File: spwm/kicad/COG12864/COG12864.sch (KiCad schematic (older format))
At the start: 62 parts, among them J1 Conn_01x02_Male, Q4 Q_NMOS_GDS, Q5 Q_NMOS_GDS, Q6 Q_NMOS_GDS, Q7 Q_NMOS_GDS, SW1 SW_Push, SW2 SW_Push, U1 N32G430C8L7, U3 EG2131, U4 EG2131, U5 LMV722, U6 LMV722, Y1 8MHZ

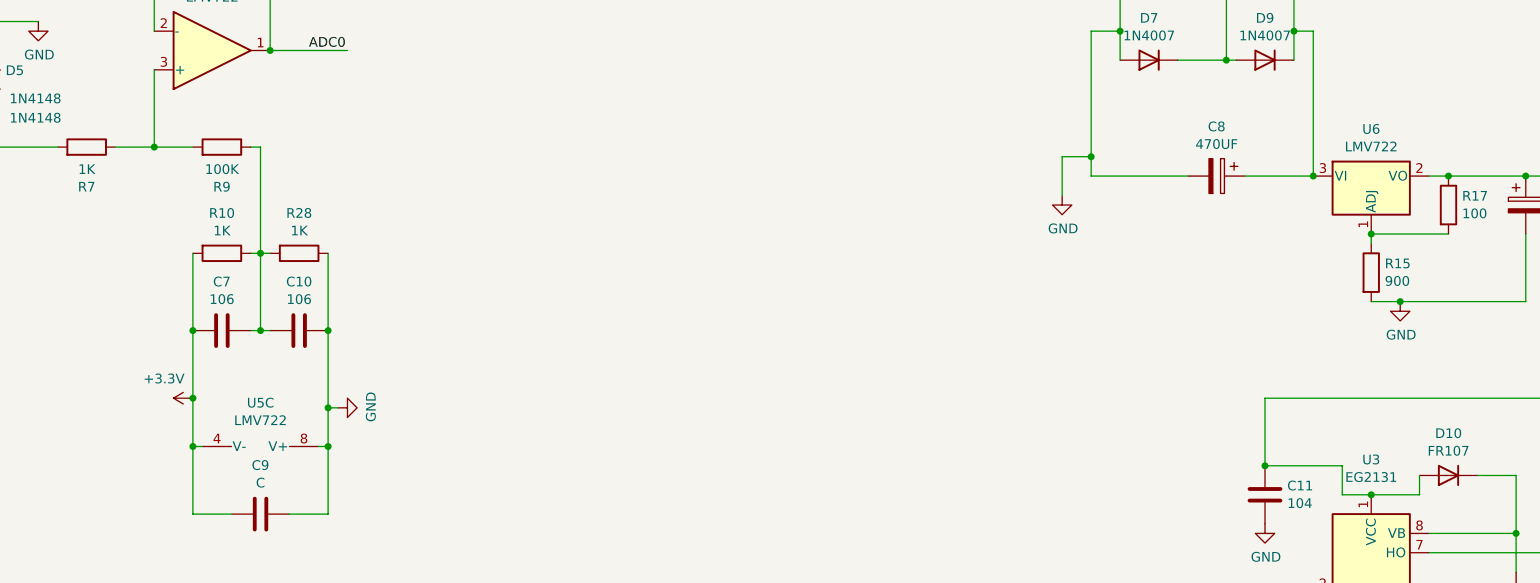
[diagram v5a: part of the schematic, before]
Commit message: 改正原理图绘制错误
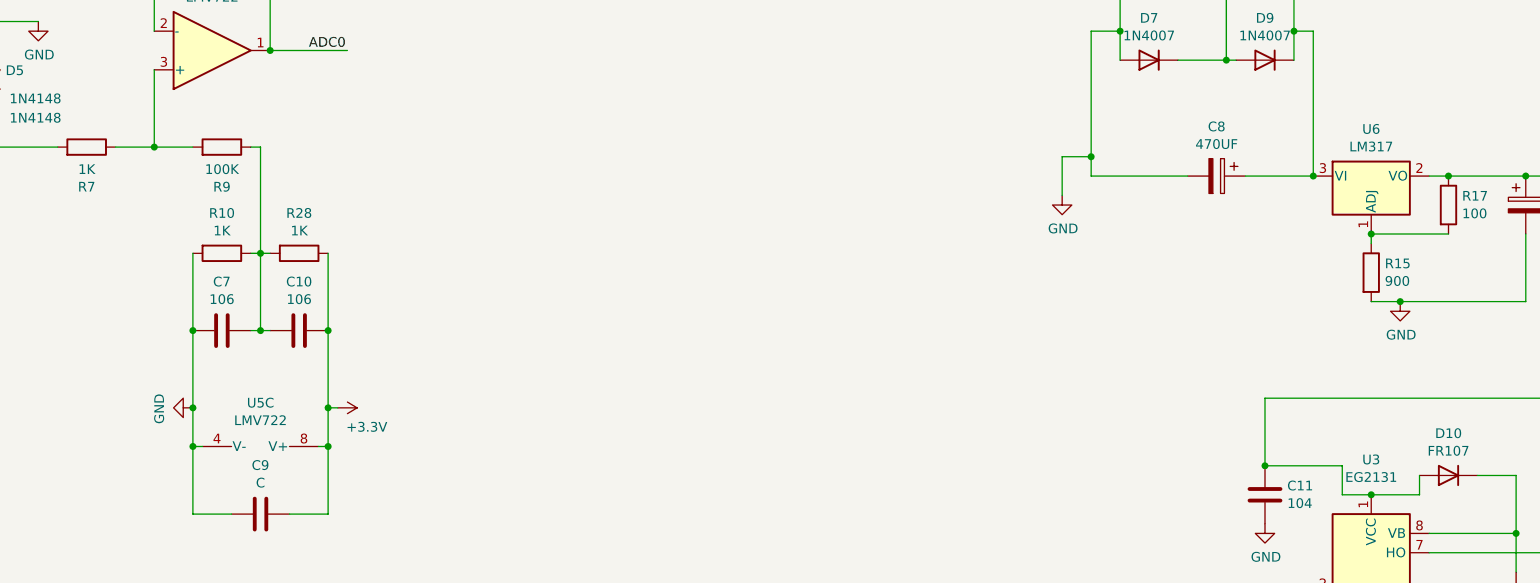
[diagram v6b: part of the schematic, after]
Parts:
- U6: value LMV722 -> LM317
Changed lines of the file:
@@
 L power:GND #PWR019
 U 1 1 62F3C1F0
+P 5350 5150
+F 0 "#PWR019" H 5350 4900 50  0001 C CNN
+F 1 "GND" H 5355 4977 50  0000 C CNN
+F 2 "" H 5350 5150 50  0001 C CNN
+F 3 "" H 5350 5150 50  0001 C CNN
+	1    5350 5150
+	0    1    1    0
+$EndComp
+$Comp
+L power:+3.3V #PWR018
+U 1 1 62F3D129
 P 6100 5150
-F 0 "#PWR019" H 6100 4900 50  0001 C CNN
-F 1 "GND" H 6105 4977 50  0000 C CNN
+F 0 "#PWR018" H 6100 5000 50  0001 C CNN
+F 1 "+3.3V" V 6200 5300 50  0000 C CNN
 F 2 "" H 6100 5150 50  0001 C CNN
 F 3 "" H 6100 5150 50  0001 C CNN
 	1    6100 5150
-	0    -1   -1   0
-$EndComp
-$Comp
-L power:+3.3V #PWR018
-U 1 1 62F3D129
-P 5350 5100
-F 0 "#PWR018" H 5350 4950 50  0001 C CNN
-F 1 "+3.3V" V 5450 5250 50  0000 C CNN
-F 2 "" H 5350 5100 50  0001 C CNN
-F 3 "" H 5350 5100 50  0001 C CNN
-	1    5350 5100
-	0    -1   -1   0
+	0    1    1    0
 $EndComp
 $Comp
@@
 Wire Wire Line
 	5400 5350 5350 5350
-Wire Wire Line
-	5350 5350 5350 5100
 Connection ~ 5350 4750
-Connection ~ 5350 5100
-Wire Wire Line
-	5350 5100 5350 4750
 $Comp
 L Device:C C9
@@
 P 11450 3950
 F 0 "U6" H 11450 4192 50  0000 C CNN
-F 1 "LMV722" H 11450 4101 50  0000 C CNN
+F 1 "LM317" H 11450 4101 50  0000 C CNN
 F 2 "" H 11450 4200 50  0001 C CIN
 F 3 "" H 11450 3950 50  0001 C CNN
@@
 Wire Wire Line
 	9950 12000 9950 12700
+Wire Wire Line
+	5350 4750 5350 5150
+Connection ~ 5350 5150
+Wire Wire Line
+	5350 5150 5350 5350
 $EndSCHEMATC

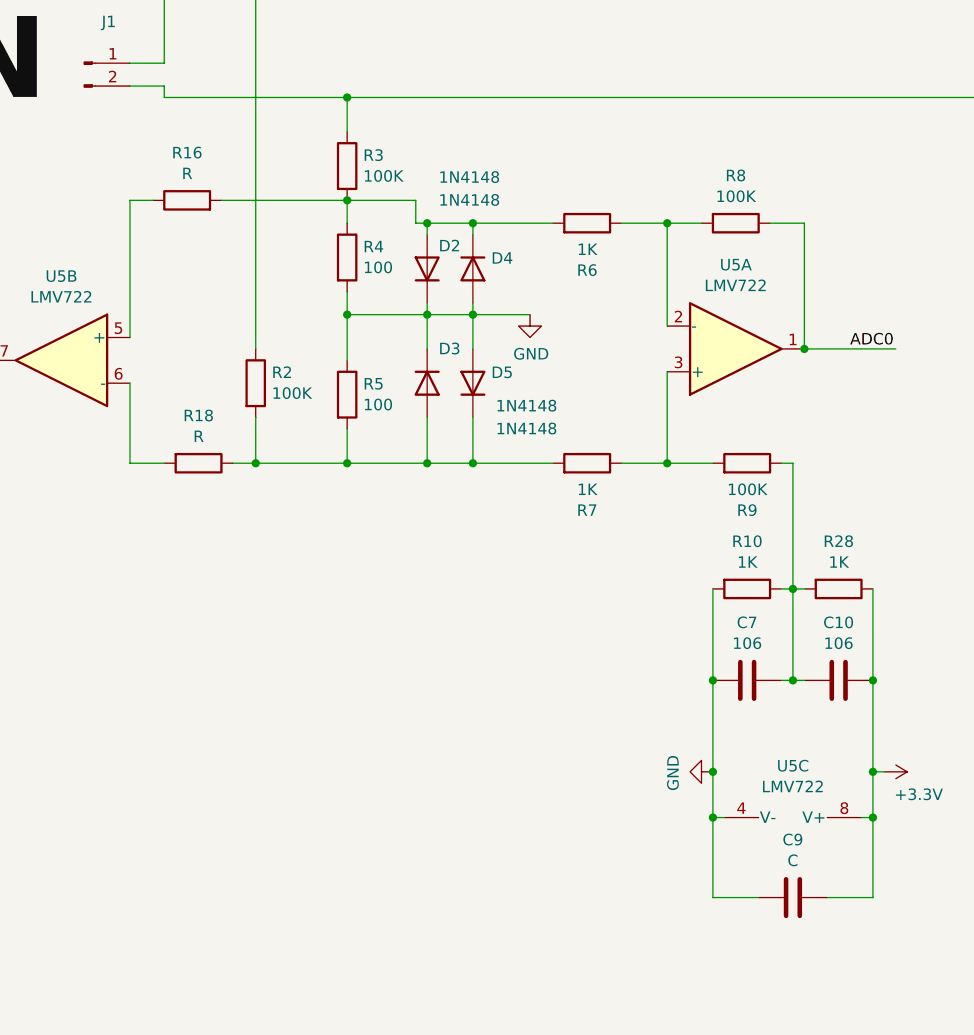
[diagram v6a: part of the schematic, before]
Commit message: 修改按键错误
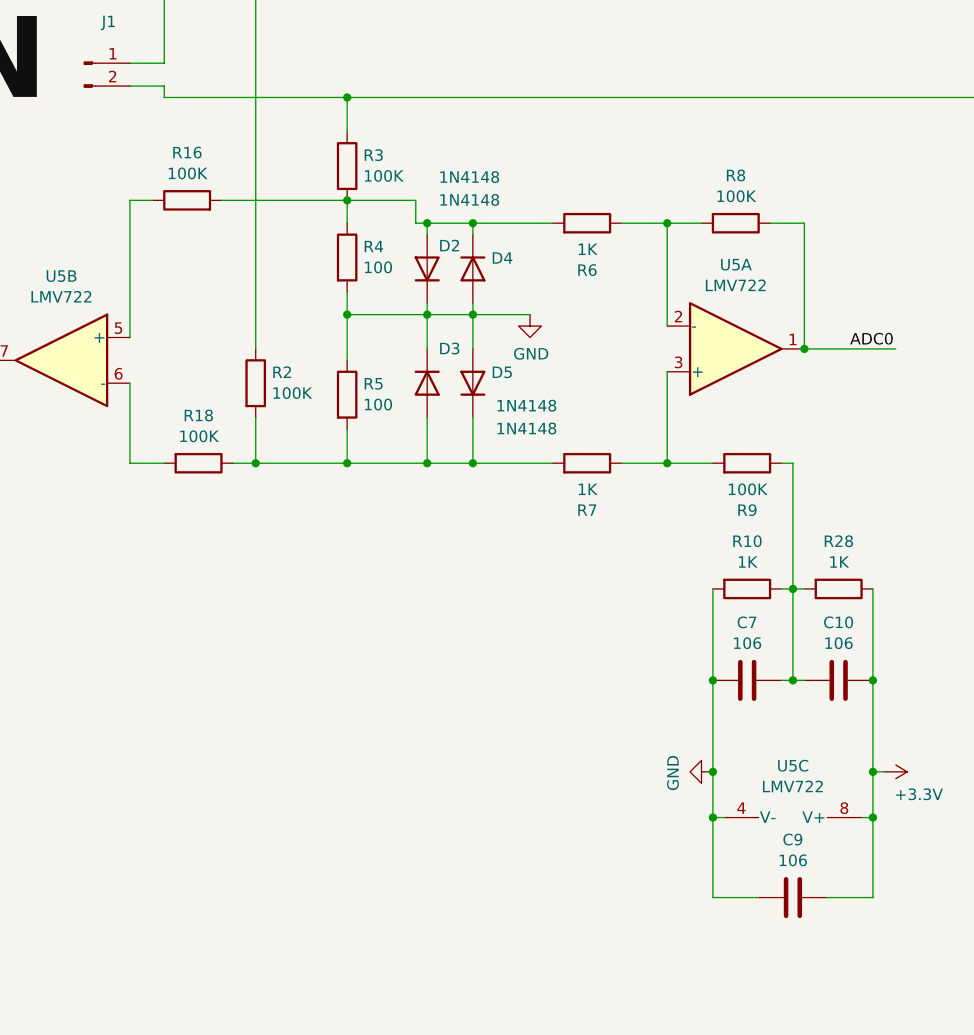
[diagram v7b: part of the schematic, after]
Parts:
- C9: value C -> 106
- R16, R18: value R -> 100K
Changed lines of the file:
@@
 P 5700 5700
 F 0 "C9" V 5448 5700 50  0000 C CNN
-F 1 "C" V 5539 5700 50  0000 C CNN
+F 1 "106" V 5539 5700 50  0000 C CNN
 F 2 "" H 5738 5550 50  0001 C CNN
 F 3 "~" H 5700 5700 50  0001 C CNN
@@
 P 3050 2650
 F 0 "R16" V 3257 2650 50  0000 C CNN
-F 1 "R" V 3166 2650 50  0000 C CNN
+F 1 "100K" V 3166 2650 50  0000 C CNN
 F 2 "" V 2980 2650 50  0001 C CNN
 F 3 "~" H 3050 2650 50  0001 C CNN
@@
 P 3100 3800
 F 0 "R18" V 2893 3800 50  0000 C CNN
-F 1 "R" V 2984 3800 50  0000 C CNN
+F 1 "100K" V 2984 3800 50  0000 C CNN
 F 2 "" V 3030 3800 50  0001 C CNN
 F 3 "~" H 3100 3800 50  0001 C CNN
